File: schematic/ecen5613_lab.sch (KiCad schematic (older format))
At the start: 20 parts, among them J4 CONN_01X09, J5 DB9_MALE, Q1 2N2907, U1 C501, U3 74LS373, U4 bq4011YMA-100, U6 ATF16V8C, Y1 11.0592MHz

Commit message: [L2] Add 74LS374 flipflop to schematic
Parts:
- added U7: 74LS374, symbol 74LS374_Flipflop
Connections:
- net labels added: DEBUG
- wire segments 141 -> 154
- no-connect marks 12 -> 20
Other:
- moved on the sheet: J4, J5
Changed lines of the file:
@@
 L DB9_MALE J5
 U 1 1 59CDD78A
-P 10150 6400
-F 0 "J5" H 10100 6950 50  0000 L CNN
-F 1 "DB9_MALE" H 9950 5800 50  0000 L CNN
-F 2 "" H 10150 6400 50  0001 C CNN
-F 3 "" H 10150 6400 50  0001 C CNN
-	1    10150 6400
+P 10100 6400
+F 0 "J5" H 10050 6950 50  0000 L CNN
+F 1 "DB9_MALE" H 9900 5800 50  0000 L CNN
+F 2 "" H 10100 6400 50  0001 C CNN
+F 3 "" H 10100 6400 50  0001 C CNN
+	1    10100 6400
 	1    0    0    1
 $EndComp
@@
 L CONN_01X09 J4
 U 1 1 59CDD78B
-P 8700 6400
-F 0 "J4" H 8650 5850 50  0000 L CNN
-F 1 "CONN_01X09" H 8778 6350 50  0001 L CNN
-F 2 "" H 8700 6400 50  0001 C CNN
-F 3 "" H 8700 6400 50  0001 C CNN
-	1    8700 6400
+P 8650 6400
+F 0 "J4" H 8600 5850 50  0000 L CNN
+F 1 "CONN_01X09" H 8728 6350 50  0001 L CNN
+F 2 "" H 8650 6400 50  0001 C CNN
+F 3 "" H 8650 6400 50  0001 C CNN
+	1    8650 6400
 	-1   0    0    -1
 $EndComp
@@
 	4100 4200 4450 4200
 Wire Wire Line
-	8900 6000 9100 6000
-Wire Wire Line
-	8900 6100 9100 6100
-Wire Wire Line
-	8900 6200 9100 6200
-Wire Wire Line
-	8900 6300 9100 6300
-Wire Wire Line
-	8900 6400 9100 6400
-Wire Wire Line
-	8900 6500 9100 6500
-Wire Wire Line
-	8900 6600 9100 6600
-Wire Wire Line
-	8900 6700 9100 6700
-Wire Wire Line
-	8900 6800 9100 6800
-Entry Wire Line
-	9100 6000 9200 6100
-Entry Wire Line
-	9100 6100 9200 6200
-Entry Wire Line
-	9100 6200 9200 6300
-Entry Wire Line
-	9100 6300 9200 6400
-Entry Wire Line
-	9100 6400 9200 6500
-Entry Wire Line
-	9100 6500 9200 6600
-Entry Wire Line
-	9100 6600 9200 6700
-Entry Wire Line
-	9100 6700 9200 6800
-Entry Wire Line
-	9100 6800 9200 6900
-Text Label 8900 6000 0    39   ~ 0
+	8850 6000 9050 6000
+Wire Wire Line
+	8850 6100 9050 6100
+Wire Wire Line
+	8850 6200 9050 6200
+Wire Wire Line
+	8850 6300 9050 6300
+Wire Wire Line
+	8850 6400 9050 6400
+Wire Wire Line
+	8850 6500 9050 6500
+Wire Wire Line
+	8850 6600 9050 6600
+Wire Wire Line
+	8850 6700 9050 6700
+Wire Wire Line
+	8850 6800 9050 6800
+Entry Wire Line
+	9050 6000 9150 6100
+Entry Wire Line
+	9050 6100 9150 6200
+Entry Wire Line
+	9050 6200 9150 6300
+Entry Wire Line
+	9050 6300 9150 6400
+Entry Wire Line
+	9050 6400 9150 6500
+Entry Wire Line
+	9050 6500 9150 6600
+Entry Wire Line
+	9050 6600 9150 6700
+Entry Wire Line
+	9050 6700 9150 6800
+Entry Wire Line
+	9050 6800 9150 6900
+Text Label 8850 6000 0    39   ~ 0
 J5P1
-Text Label 8900 6100 0    39   ~ 0
+Text Label 8850 6100 0    39   ~ 0
 J5P2
-Text Label 8900 6200 0    39   ~ 0
+Text Label 8850 6200 0    39   ~ 0
 J5P3
-Text Label 8900 6300 0    39   ~ 0
+Text Label 8850 6300 0    39   ~ 0
 J5P4
-Text Label 8900 6400 0    39   ~ 0
+Text Label 8850 6400 0    39   ~ 0
 J5P5
-Text Label 8900 6500 0    39   ~ 0
+Text Label 8850 6500 0    39   ~ 0
 J5P6
-Text Label 8900 6600 0    39   ~ 0
+Text Label 8850 6600 0    39   ~ 0
 J5P7
-Text Label 8900 6700 0    39   ~ 0
+Text Label 8850 6700 0    39   ~ 0
 J5P8
-Text Label 8900 6800 0    39   ~ 0
+Text Label 8850 6800 0    39   ~ 0
 J5P9
-Text Label 9850 6000 2    39   ~ 0
+Text Label 9800 6000 2    39   ~ 0
 J5P1
-Text Label 9850 6200 2    39   ~ 0
+Text Label 9800 6200 2    39   ~ 0
 J5P2
-Text Label 9850 6400 2    39   ~ 0
+Text Label 9800 6400 2    39   ~ 0
 J5P3
-Text Label 9850 6600 2    39   ~ 0
+Text Label 9800 6600 2    39   ~ 0
 J5P4
-Text Label 9850 6800 2    39   ~ 0
+Text Label 9800 6800 2    39   ~ 0
 J5P5
-Text Label 9850 6100 2    39   ~ 0
+Text Label 9800 6100 2    39   ~ 0
 J5P6
-Text Label 9850 6300 2    39   ~ 0
+Text Label 9800 6300 2    39   ~ 0
 J5P7
-Text Label 9850 6500 2    39   ~ 0
+Text Label 9800 6500 2    39   ~ 0
 J5P8
-Text Label 9850 6700 2    39   ~ 0
+Text Label 9800 6700 2    39   ~ 0
 J5P9
 Wire Wire Line
-	9850 6000 9700 6000
-Wire Wire Line
-	9850 6100 9700 6100
-Wire Wire Line
-	9850 6200 9700 6200
-Wire Wire Line
-	9850 6300 9700 6300
-Wire Wire Line
-	9850 6400 9700 6400
-Wire Wire Line
-	9850 6500 9700 6500
-Wire Wire Line
-	9850 6600 9700 6600
-Wire Wire Line
-	9850 6700 9700 6700
-Wire Wire Line
-	9850 6800 9700 6800
-Entry Wire Line
-	9700 6000 9600 6100
-Entry Wire Line
-	9700 6100 9600 6200
-Entry Wire Line
-	9700 6200 9600 6300
-Entry Wire Line
-	9700 6300 9600 6400
-Entry Wire Line
-	9700 6400 9600 6500
-Entry Wire Line
-	9700 6500 9600 6600
-Entry Wire Line
-	9700 6600 9600 6700
-Entry Wire Line
-	9700 6700 9600 6800
-Entry Wire Line
-	9700 6800 9600 6900
-Wire Bus Line
-	9600 6100 9600 6900
-Wire Bus Line
-	9200 6100 9200 6900
-Wire Bus Line
-	9200 6100 9600 6100
-Text Label 9250 6100 0    39   ~ 0
+	9800 6000 9650 6000
+Wire Wire Line
+	9800 6100 9650 6100
+Wire Wire Line
+	9800 6200 9650 6200
+Wire Wire Line
+	9800 6300 9650 6300
+Wire Wire Line
+	9800 6400 9650 6400
+Wire Wire Line
+	9800 6500 9650 6500
+Wire Wire Line
+	9800 6600 9650 6600
+Wire Wire Line
+	9800 6700 9650 6700
+Wire Wire Line
+	9800 6800 9650 6800
+Entry Wire Line
+	9650 6000 9550 6100
+Entry Wire Line
+	9650 6100 9550 6200
+Entry Wire Line
+	9650 6200 9550 6300
+Entry Wire Line
+	9650 6300 9550 6400
+Entry Wire Line
+	9650 6400 9550 6500
+Entry Wire Line
+	9650 6500 9550 6600
+Entry Wire Line
+	9650 6600 9550 6700
+Entry Wire Line
+	9650 6700 9550 6800
+Entry Wire Line
+	9650 6800 9550 6900
+Wire Bus Line
+	9550 6100 9550 6900
+Wire Bus Line
+	9150 6100 9150 6900
+Wire Bus Line
+	9150 6100 9550 6100
+Text Label 9200 6100 0    39   ~ 0
 J5P[1..9]
 Text Label 4200 3300 0    39   ~ 0
@@
 Wire Bus Line
 	4650 2050 4550 1950
+$Comp
+L 74LS374_Flipflop U7
+U 1 1 59D1FBF3
+P 9150 2350
+F 0 "U7" H 9450 2350 60  0000 C CNN
+F 1 "74LS374" H 9450 2250 60  0000 C CNN
+F 2 "" H 9150 2350 60  0001 C CNN
+F 3 "" H 9150 2350 60  0001 C CNN
+	1    9150 2350
+	1    0    0    -1
+$EndComp
+Wire Wire Line
+	8950 3400 8900 3400
+Wire Wire Line
+	8900 3400 8900 3600
+Wire Wire Line
+	8900 3600 9450 3600
+$Comp
+L GND #PWR?
+U 1 1 59D1FFDB
+P 9450 3600
+F 0 "#PWR?" H 9450 3350 50  0001 C CNN
+F 1 "GND" H 9455 3427 50  0000 C CNN
+F 2 "" H 9450 3600 50  0001 C CNN
+F 3 "" H 9450 3600 50  0001 C CNN
+	1    9450 3600
+	1    0    0    -1
+$EndComp
+Entry Wire Line
+	8650 1950 8750 2050
+Entry Wire Line
+	8650 2100 8750 2200
+Entry Wire Line
+	8650 2250 8750 2350
+Entry Wire Line
+	8650 2400 8750 2500
+Entry Wire Line
+	8650 2550 8750 2650
+Entry Wire Line
+	8650 2700 8750 2800
+Entry Wire Line
+	8650 2850 8750 2950
+Entry Wire Line
+	8650 3000 8750 3100
+Text Label 8800 2050 0    39   ~ 0
+AD0
+Text Label 8800 2200 0    39   ~ 0
+AD1
+Text Label 8800 2350 0    39   ~ 0
+AD2
+Text Label 8800 2500 0    39   ~ 0
+AD3
+Text Label 8800 2650 0    39   ~ 0
+AD4
+Text Label 8800 2800 0    39   ~ 0
+AD5
+Text Label 8800 2950 0    39   ~ 0
+AD6
+Text Label 8800 3100 0    39   ~ 0
+AD7
+Wire Wire Line
+	8750 2050 8950 2050
+Wire Wire Line
+	8750 2200 8950 2200
+Wire Wire Line
+	8750 2350 8950 2350
+Wire Wire Line
+	8750 2500 8950 2500
+Wire Wire Line
+	8750 2650 8950 2650
+Wire Wire Line
+	8750 2800 8950 2800
+Wire Wire Line
+	8750 2950 8950 2950
+Wire Wire Line
+	8750 3100 8950 3100
+Text GLabel 6550 6300 2    39   Input ~ 0
+DEBUG
+Wire Wire Line
+	6450 6300 6550 6300
+Text GLabel 8950 3250 0    39   Input ~ 0
+DEBUG
+Text GLabel 9450 1800 1    39   Input ~ 0
+VCC
+Wire Wire Line
+	9450 1800 9450 1850
+NoConn ~ 9950 2200
+NoConn ~ 9950 2350
+NoConn ~ 9950 2500
+NoConn ~ 9950 2650
+NoConn ~ 9950 2800
+NoConn ~ 9950 2950
+NoConn ~ 9950 3100
+NoConn ~ 9950 3250
 $EndSCHEMATC

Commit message: Add debug and serial schematics, update for AT89C51
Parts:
- removed J4: CONN_01X09, symbol CONN_01X09
- removed J5: DB9_MALE, symbol DB9_MALE
- removed U1: C501, symbol C501
- removed U7: 74LS374, symbol 74LS374_Flipflop
- added R?: 1000, symbol R
- added SW3: Bootloader, symbol SW_Push
- added U1: AT89C51RC2, symbol AT89C51RC2
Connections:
- net labels removed: J5P1, J5P2, J5P3, J5P4, J5P5, J5P6, J5P7, J5P8, J5P9, J5P[1..9]
- wire segments 154 -> 128
- no-connect marks 20 -> 6
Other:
- note added: "(SPLD code: lab.pld)"
- moved on the sheet: C20, C21, C22, C5, C6, D8, Q1, R4, R5, U3, U4, U6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

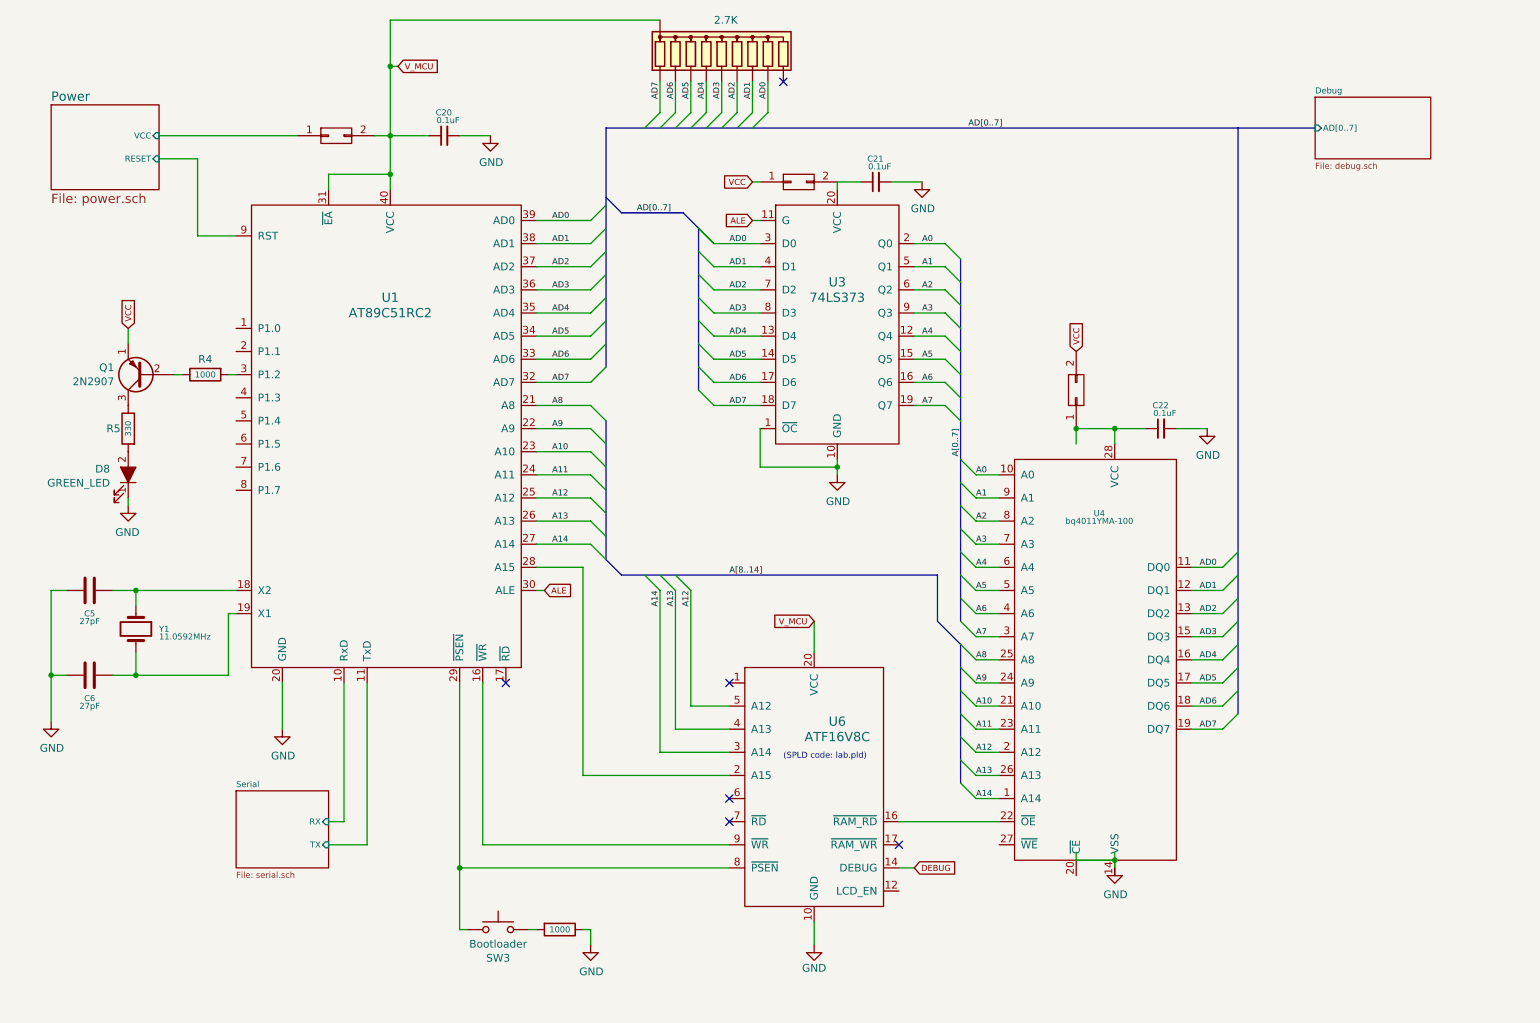
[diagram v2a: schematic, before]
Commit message: [L3] Update schematic with new NVRAM signals
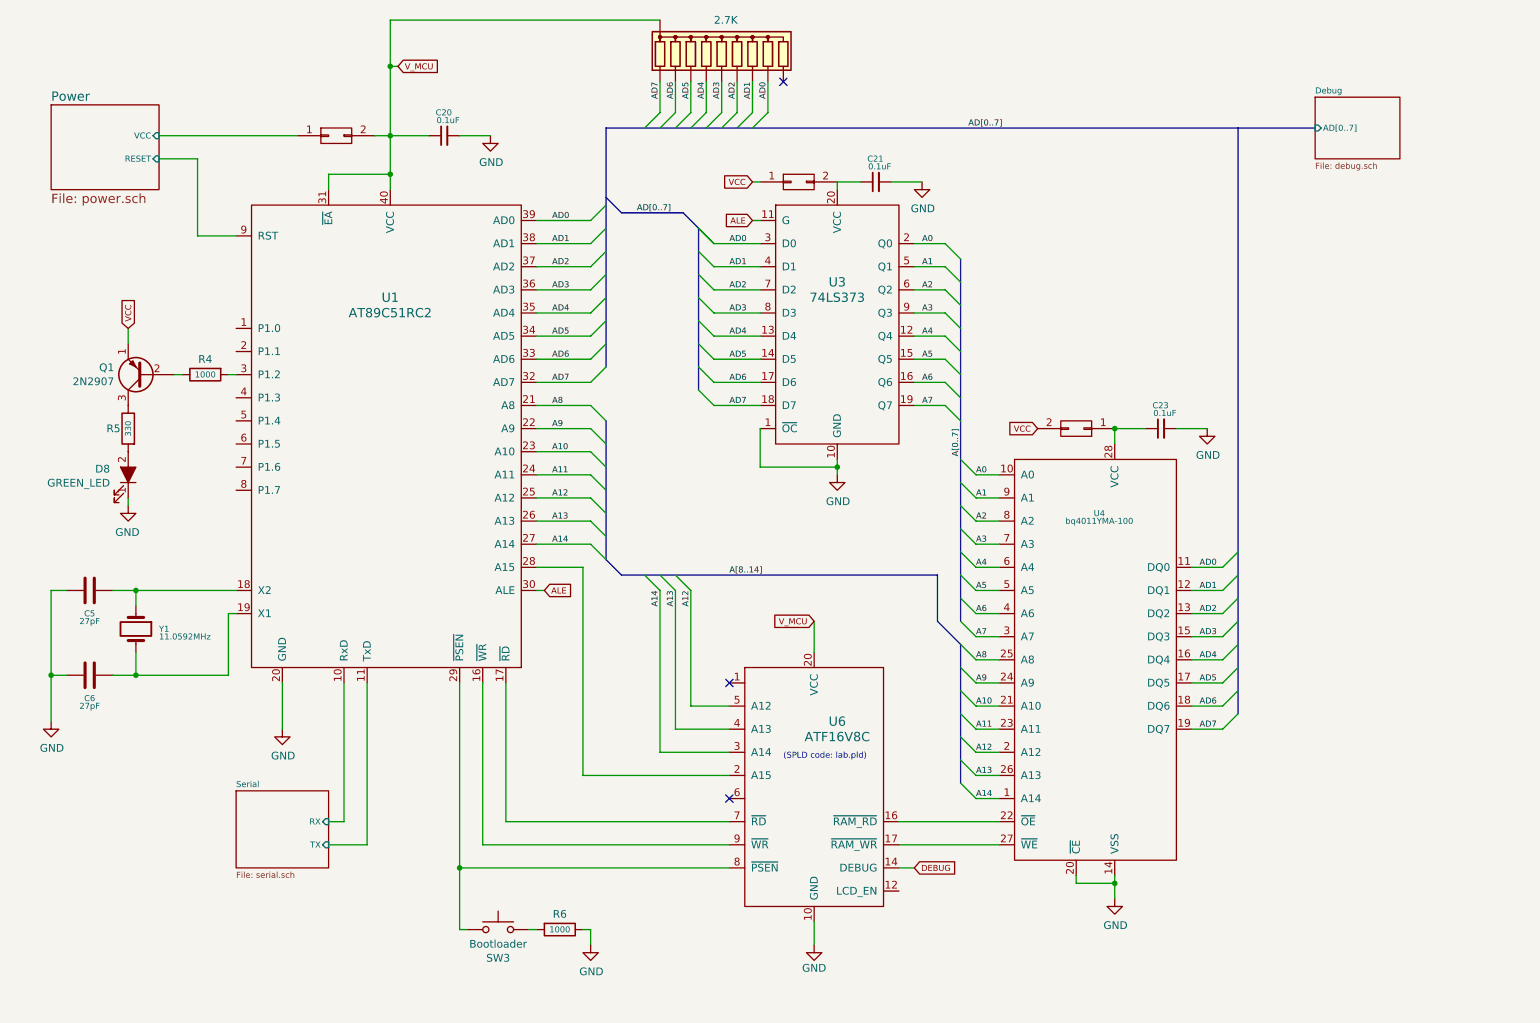
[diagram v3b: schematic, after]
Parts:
- gave numbers to parts that had none: 1
- renumbered C22 to C23
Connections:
- net GND: now also U4.14 (VSS), U4.20 (~CE)
- net at U6.17 (~RAM_WR): now also U4.27 (~WE)
- net at U6.7 (~RD): now also U1.17 (~RD)
- no-connect marks 6 -> 3
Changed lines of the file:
@@
 L CONN_02X01 J?
 U 1 1 59CDD785
-P 7450 3200
-F 0 "J?" H 7450 3415 50  0001 C CNN
-F 1 "CONN_02X01" H 7450 3324 50  0001 C CNN
-F 2 "" H 7450 2000 50  0001 C CNN
-F 3 "" H 7450 2000 50  0001 C CNN
-	1    7450 3200
-	0    -1   -1   0
-$EndComp
-Text GLabel 7450 2950 1    39   Input ~ 0
+P 7450 3450
+F 0 "J?" H 7450 3665 50  0001 C CNN
+F 1 "CONN_02X01" H 7450 3574 50  0001 C CNN
+F 2 "" H 7450 2250 50  0001 C CNN
+F 3 "" H 7450 2250 50  0001 C CNN
+	1    7450 3450
+	-1   0    0    1
+$EndComp
+Text GLabel 7200 3450 0    39   Input ~ 0
 VCC
 $Comp
@@
 L GND #PWR?
 U 1 1 59CE9B17
-P 7700 6300
-F 0 "#PWR?" H 7700 6050 50  0001 C CNN
-F 1 "GND" H 7705 6127 50  0000 C CNN
-F 2 "" H 7700 6300 50  0001 C CNN
-F 3 "" H 7700 6300 50  0001 C CNN
-	1    7700 6300
+P 7700 6500
+F 0 "#PWR?" H 7700 6250 50  0001 C CNN
+F 1 "GND" H 7705 6327 50  0000 C CNN
+F 2 "" H 7700 6500 50  0001 C CNN
+F 3 "" H 7700 6500 50  0001 C CNN
+	1    7700 6500
 	1    0    0    -1
 $EndComp
@@
 $EndComp
 $Comp
-L C_Small C22
+L C_Small C23
 U 1 1 59CEAE5E
 P 8000 3450
-F 0 "C22" V 8150 3400 39  0000 L CNN
+F 0 "C23" V 8150 3400 39  0000 L CNN
 F 1 "0.1uF" V 8100 3350 39  0000 L CNN
 F 2 "" H 8000 3450 50  0001 C CNN
@@
 NoConn ~ 5200 5100
 NoConn ~ 5200 5850
-NoConn ~ 6300 6150
 Text Label 4950 4500 3    39   ~ 0
 A12
@@
 	8200 5400 8400 5400
 Wire Wire Line
-	7450 3550 7450 3450
-Wire Wire Line
-	7450 6200 7450 6250
-Wire Wire Line
-	7450 6250 7700 6250
-Wire Wire Line
-	7700 6200 7700 6300
-Connection ~ 7700 6250
-Wire Wire Line
 	2900 1550 3250 1550
 Wire Wire Line
@@
 	8100 3450 8300 3450
 Wire Wire Line
-	7450 3450 7900 3450
+	7700 3450 7900 3450
 Wire Wire Line
 	3950 3900 4300 3900
@@
 	7700 3450 7700 3550
 Connection ~ 7700 3450
-Connection ~ 7450 3450
 Wire Bus Line
 	4500 2050 4900 2050
@@
 	6300 6300 6400 6300
 $Sheet
-S 9000 1300 750  400
+S 9000 1300 550  400
 U 59D6D316
 F0 "Debug" 39
@@
 	1    0    0    -1
 $EndComp
-NoConn ~ 5200 6000
 Wire Wire Line
 	3600 5100 3600 6150
@@
 Wire Wire Line
 	3450 5100 3450 6700
-NoConn ~ 3750 5100
 $Comp
 L SW_Push SW3
@@
 Connection ~ 3450 6300
 $Comp
-L R R?
+L R R6
 U 1 1 59DE66D4
 P 4100 6700
-F 0 "R?" V 3909 6700 50  0001 C CNN
+F 0 "R6" V 4000 6700 50  0000 C CNN
 F 1 "1000" V 4100 6700 39  0000 C CNN
 F 2 "" V 4030 6700 50  0001 C CNN
@@
 	2600 1800 3000 1800
 Connection ~ 3000 1800
+Wire Wire Line
+	5200 6000 3750 6000
+Wire Wire Line
+	3750 6000 3750 5100
+Wire Wire Line
+	7450 6350 7450 6400
+Wire Wire Line
+	7450 6400 7700 6400
+Wire Wire Line
+	7700 6350 7700 6500
+Connection ~ 7700 6400
+Wire Wire Line
+	6950 6150 6300 6150
 $EndSCHEMATC
